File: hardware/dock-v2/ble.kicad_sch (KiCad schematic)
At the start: 0 parts

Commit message: Dock v2: all parts placed on their sheets (not wired)
149 parts across POWER, USB_PORTS, MCU_A, MCU_B, BLE and POGO (A3), in
labelled groups, with references (sheet x 100), values, footprints, LCSC
numbers (hidden LCSC field) and a Note per part. Only unconnected-pin ERC
messages remain.

5 V buck values from TI's TPS54331 Table 7-1 (5 V design), moved to Basic
parts: 12k/2.2k feedback (5.16 V), 51k + 4.7nF + 47pF compensation, 10 nF
soft start, 3 x 22 uF out; recorded in docs/dock-v2-power-input.md.
New footprint dock_v2:CP_Radial_D6.3mm_P5.00mm for the hand-soldered 220 uF.

Co-Authored-By: Claude Opus 5.5 <noreply@anthropic.com>
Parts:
- added C501: 1uF, Capacitor_SMD:C_0402_1005Metric, symbol Device:C
- added C502: 10uF, Capacitor_SMD:C_0805_2012Metric, symbol Device:C
- added C503: 100nF, Capacitor_SMD:C_0402_1005Metric, symbol Device:C
- added R501, R502, R503: 10k, Resistor_SMD:R_0402_1005Metric, symbol Device:R
- added TP501, TP502, TP503, TP504, TP505: TestPoint, TestPoint:TestPoint_Pad_D1.0mm, symbol Connector:TestPoint
- added U501: ESP32-C3-MINI-1-H4X, dock_v2:ESP32-C3-MINI-1, symbol dock_v2_custom:ESP32-C3-MINI-1
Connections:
- new net: U501.1 (GND), U501.11 (GND), U501.14 (GND), U501.2 (GND), U501.36 (GND), U501.37 (GND), U501.38 (GND), U501.39 (GND), U501.40 (GND), U501.41 (GND), U501.42 (GND), U501.43 (GND), U501.44 (GND), U501.45 (GND), U501.46 (GND), U501.47 (GND), U501.48 (GND), U501.49 (GND), U501.50 (GND), U501.51 (GND), U501.52 (GND), U501.53 (GND)
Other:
- note added: "ESP32-C3-MINI-1 (antenna at the left edge)"
- note added: "Reset / boot straps"
- note added: "Test pads (fallback flashing)"

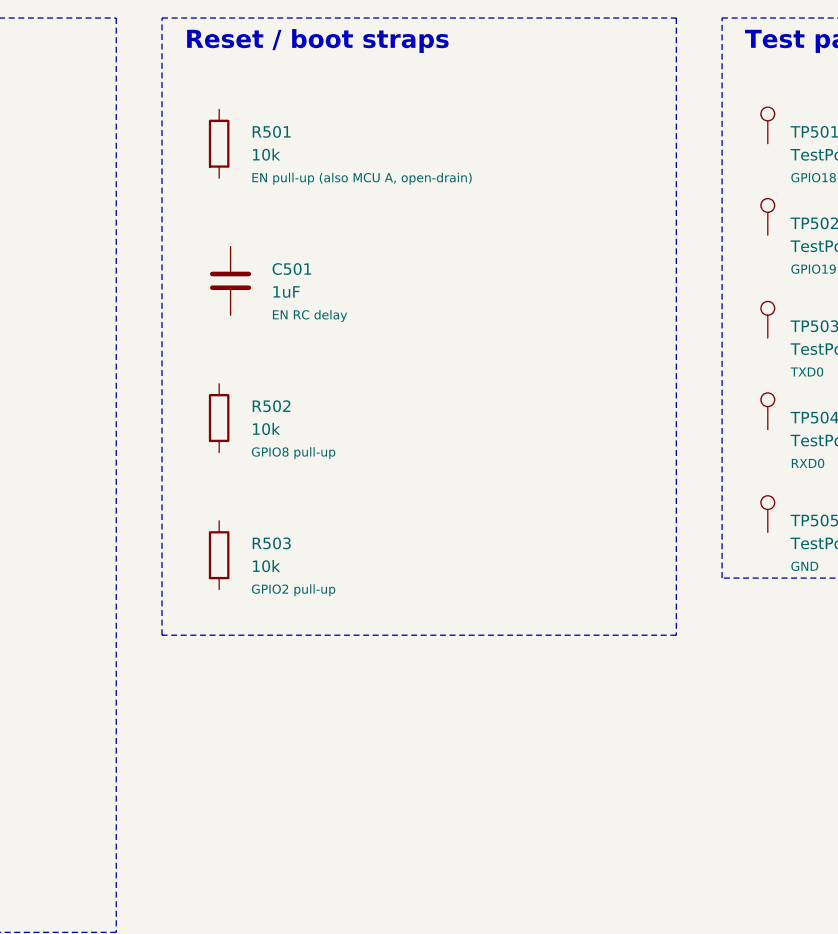
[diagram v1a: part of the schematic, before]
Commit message: Dock v2: connection guide (DOCK_CONNECTIONS.md), pin maps, wiring checker
hardware/dock-v2/DOCK_CONNECTIONS.md, in the style of the pad's guide: per
sheet a sketch, parts table (value, footprint, LCSC, job), pin-by-pin wiring
tables, placement notes; MCU A/B pin maps; nets that cross sheets (global
labels); PWR_FLAG and no-connect lists; full net index. Tables are generated
from one connection model (tools/dock_v2_connections/dock_nets.py) that is
checked against the placed schematic: 570 pins, each on a net or NC exactly once.

Found while making the pin map: MCU A's pins are weak pull-downs at reset, so
added 10k pull-ups on B_RUN, B_BOOTSEL (R406, R407) and ESP32 GPIO9 (R504),
and POGO_OFF now drives its own 2N7002 (Q602, R609) so a blank MCU A can't
switch off pad charging. 154 parts.

tools/dock_v2_connections/check_wiring.py compares the wired schematic with
the guide (unwired / split / merged / NC); make_doc.py regenerates the guide.

Co-Authored-By: Claude Opus 5.5 <noreply@anthropic.com>
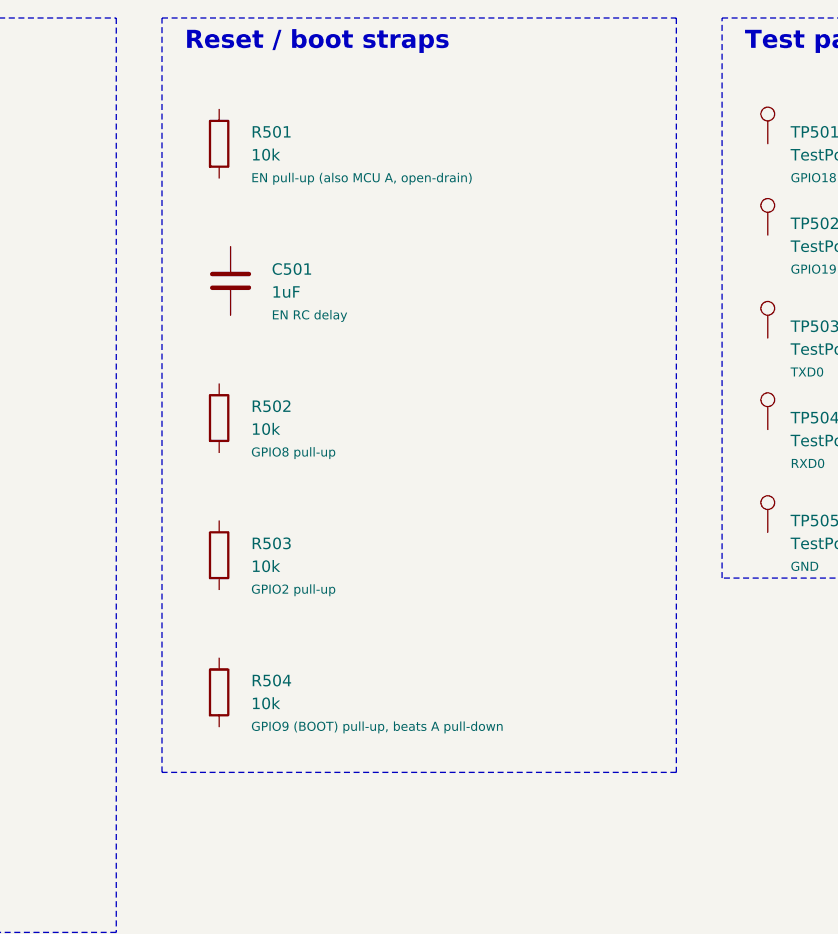
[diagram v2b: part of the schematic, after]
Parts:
- added R504: 10k, Resistor_SMD:R_0402_1005Metric, symbol Device:R
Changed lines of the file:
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@@
 	(rectangle
 		(start 125.73 17.78)
-		(end 182.88 86.36)
+		(end 182.88 101.60)
 		(stroke
 			(width 0)
@@
 					(unit 1)
 				)
+			)
+		)
+	)
+	(symbol
+		(lib_id "Device:R")
+		(at 132.08 92.71 0)
+		(unit 1)
+		(body_style 1)
+		(exclude_from_sim no)
+		(in_bom yes)
+		(on_board yes)
+		(in_pos_files yes)
+		(dnp no)
+		(fields_autoplaced no)
+		(property "Reference" "R504"
+			(at 135.64 91.44 0)
+			(show_name no)
+			(do_not_autoplace no)
+			(effects
+				(font
+					(size 1.27 1.27)
+				)
+				(justify left)
+			)
+		)
+		(property "Value" "10k"
+			(at 135.64 93.98 0)
+			(show_name no)
+			(do_not_autoplace no)
+			(effects
+				(font
+					(size 1.27 1.27)
+				)
+				(justify left)
+			)
+		)
+		(property "Footprint" "Resistor_SMD:R_0402_1005Metric"
+			(at 132.08 92.71 0)
+			(hide yes)
+			(show_name no)
+			(do_not_autoplace no)
+			(effects
+				(font
+					(size 1.27 1.27)
+				)
+			)
+		)
+		(property "Datasheet" ""
+			(at 132.08 92.71 0)
+			(hide yes)
+			(show_name no)
+			(do_not_autoplace no)
+			(effects
+				(font
+					(size 1.27 1.27)
+				)
+			)
+		)
+		(property "Description" "Resistor"
+			(at 132.08 92.71 0)
+			(hide yes)
+			(show_name no)
+			(do_not_autoplace no)
+			(effects
+				(font
+					(size 1.27 1.27)
+				)
+			)
+		)
+		(property "LCSC" "C25744"
+			(at 132.08 92.71 0)
+			(hide yes)
+			(show_name no)
+			(do_not_autoplace no)
+			(effects
+				(font
+					(size 1.27 1.27)
+				)
+			)
+		)
+		(property "Note" "GPIO9 (BOOT) pull-up, beats A pull-down"
+			(at 135.64 96.52 0)
+			(show_name no)
+			(do_not_autoplace no)
+			(effects
+				(font
+					(size 1.0 1.0)
+				)
+				(justify left)
+			)
+		)
+		(pin "1"
+		)
+		(pin "2"
+		)
+		(instances
+			(project "dock-v2"
+				(path "/928a9dc6-b0ce-4f47-a17d-f26fd77e396a/5e723931-1b1f-4c1f-9dbd-4e86e488dec2"
+					(reference "R504")
+					(unit 1)
+				)
